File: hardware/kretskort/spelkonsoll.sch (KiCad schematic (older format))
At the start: 18 parts, among them SW1 SW_Push, SW2 SW_Push, SW3 SW_Push, SW4 SW_Push, SW5 SW_Push, SW6 SW_Push, SW7 SW_Push, SW8 SW_Push, U1 ESP32-DEVKITC-32D, U2 ILI9488

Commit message: update KiCad files
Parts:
- removed SW1, SW2, SW3, SW4, SW5, SW6, SW7, SW8: SW_Push, footprints:B3F1052, symbol spelkonsoll-rescue:SW_Push-Switch
- added SW1, SW2, SW3, SW4, SW5, SW6, SW7, SW8: B3F-1052, footprints:Button, symbol Button:B3F-1052
- added U3: 1043, footprints:18650holder, symbol 18650holder:1043
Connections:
- net +5V: now also SW1.3, SW2.3, SW3.3, SW4.3, SW5.3, SW6.3, SW7.3, SW8.3, U3.1
- net BTN_A: now also SW5.1
- net BTN_B: now also SW6.1
- net BTN_DP_DOWN: now also SW2.1
- net BTN_DP_LEFT: now also SW3.1
- net BTN_DP_RIGHT: now also SW4.1
- net BTN_DP_UP: now also SW1.1
- net BTN_X: now also SW7.1
- net BTN_Y: now also SW8.1
- net GND: now also U3.2
- no-connect marks 29 -> 45
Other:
- note added: "18650 BATTERY"
- note added: "BUTTONS"
- note removed: "BUTTONS ’N"
- moved on the sheet: R1, U1, U2

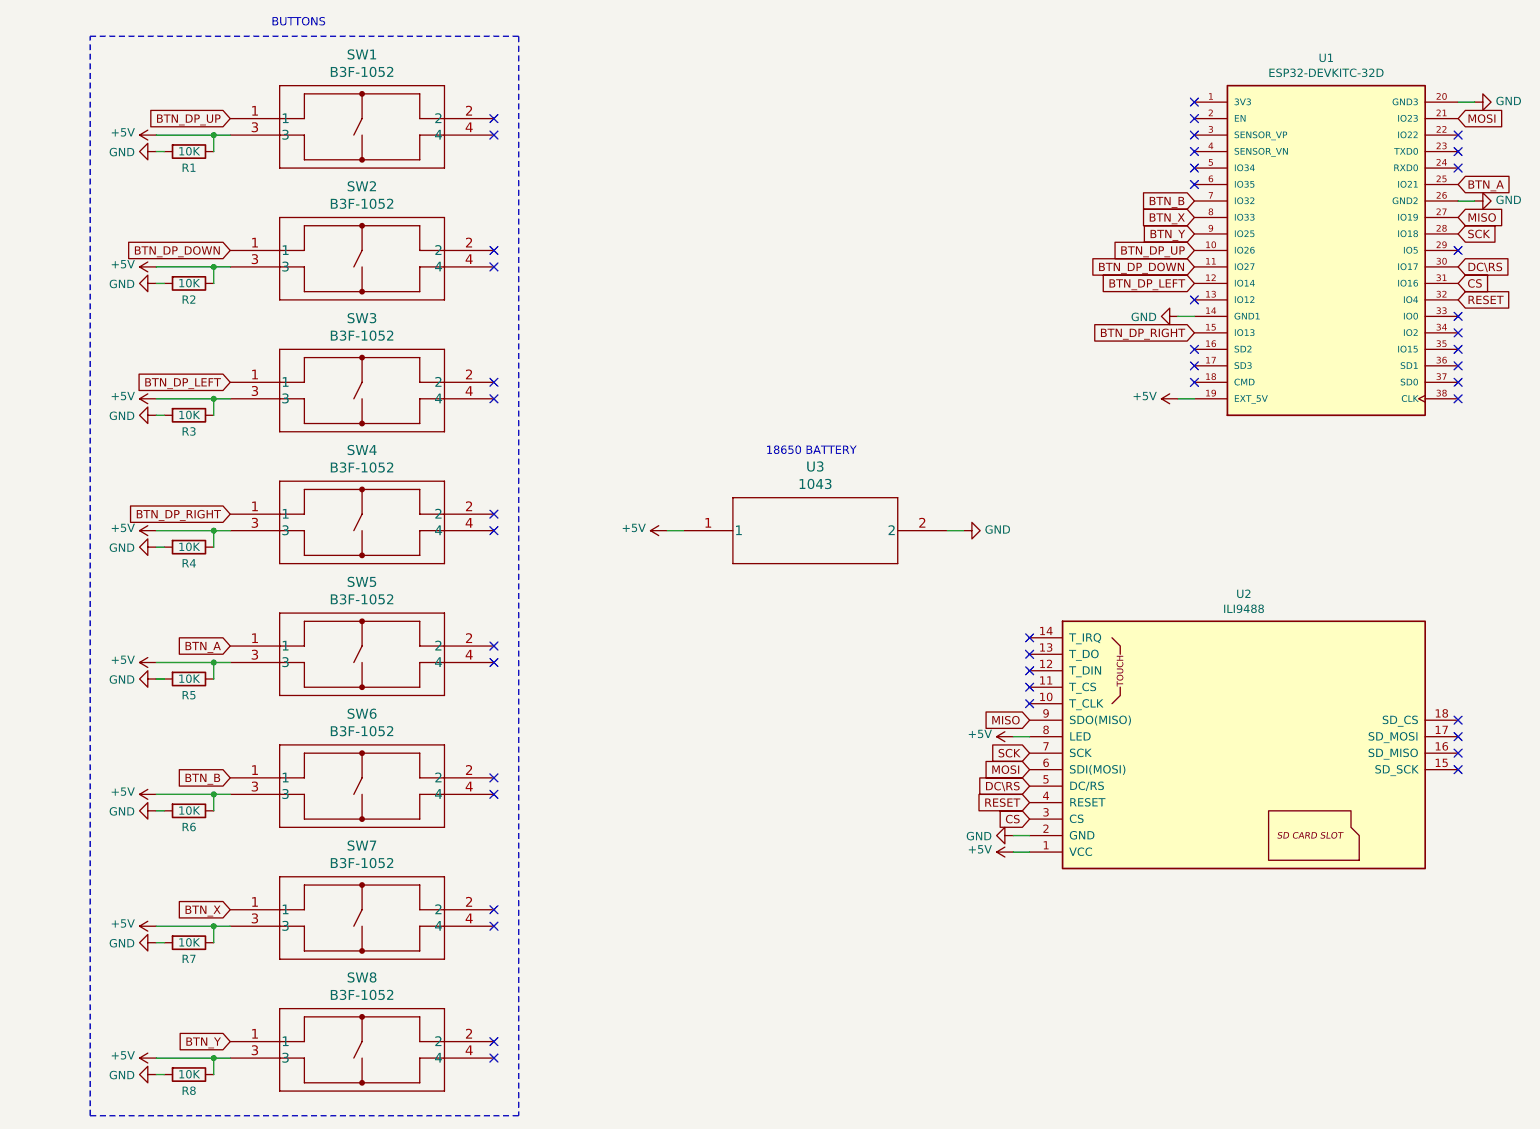
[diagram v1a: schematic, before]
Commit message: update schematic and footprints
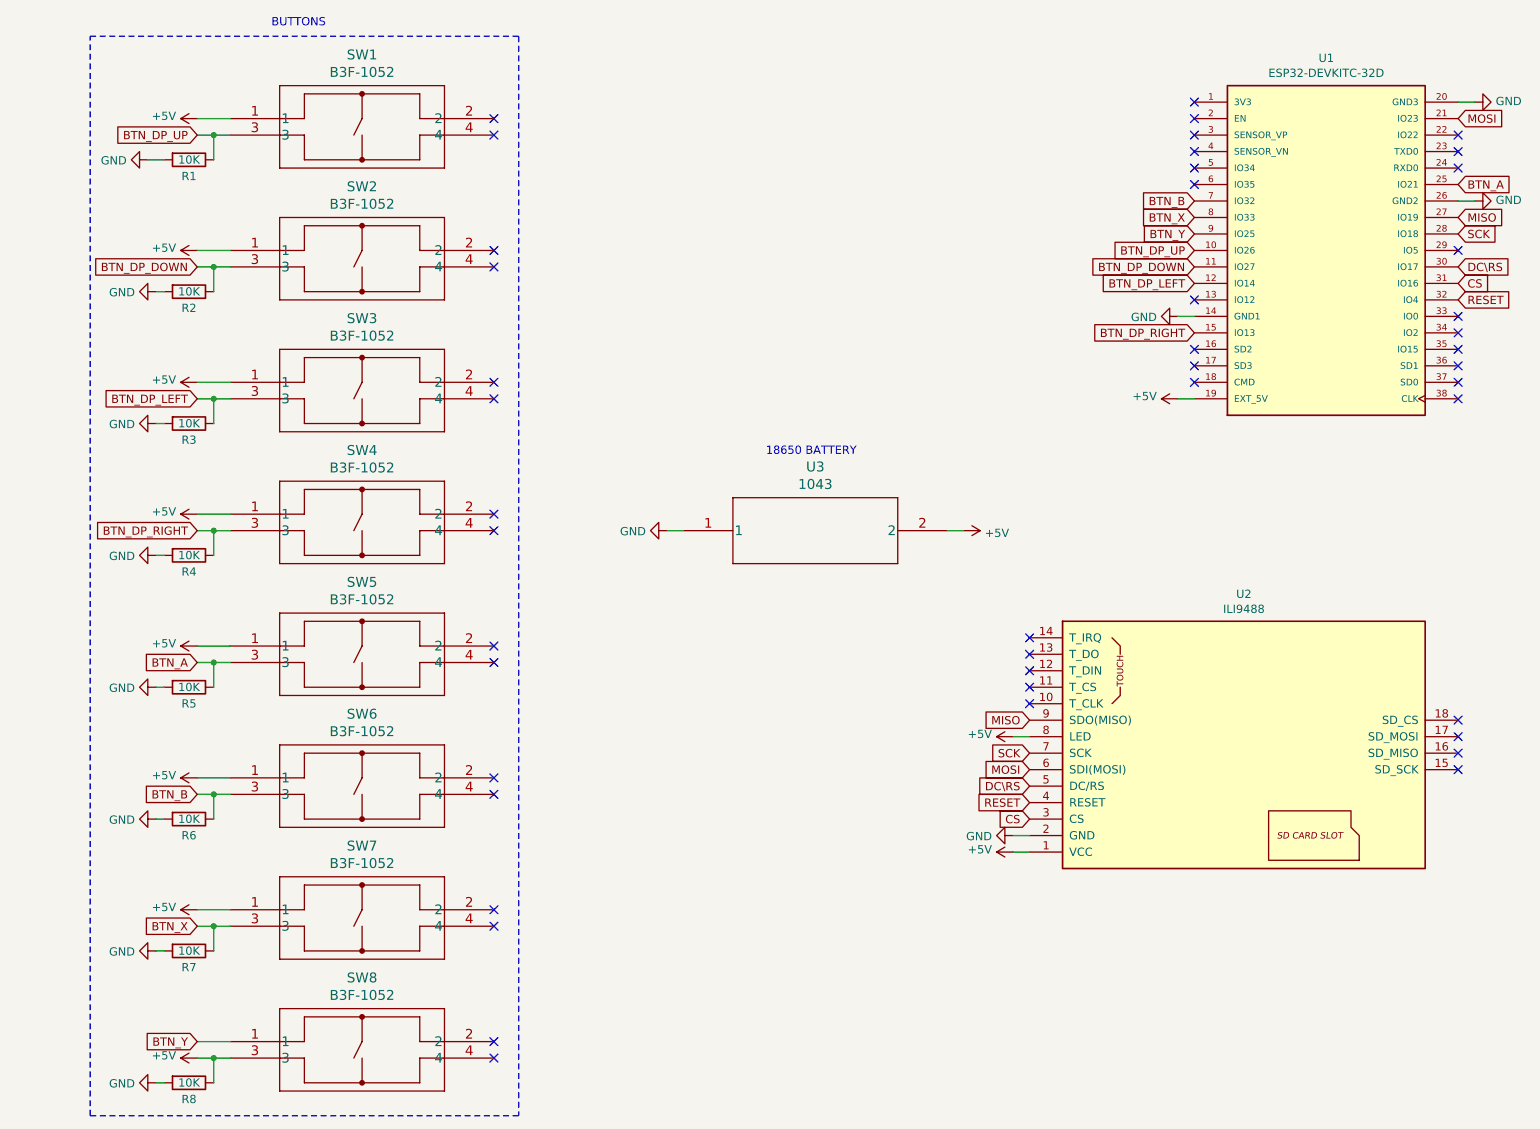
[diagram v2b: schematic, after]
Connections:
- net +5V: now also SW1.1, SW2.1, SW3.1, SW4.1, SW5.1, SW6.1, SW7.1, U3.2; no longer R1.1, R2.1, R3.1, R4.1, R5.1, R6.1, R7.1, SW1.3, SW2.3, SW3.3, SW4.3, SW5.3, SW6.3, SW7.3, U3.1
- net BTN_A: now also R5.1, SW5.3; no longer SW5.1
- net BTN_B: now also R6.1, SW6.3; no longer SW6.1
- net BTN_DP_DOWN: now also R2.1, SW2.3; no longer SW2.1
- net BTN_DP_LEFT: now also R3.1, SW3.3; no longer SW3.1
- net BTN_DP_RIGHT: now also R4.1, SW4.3; no longer SW4.1
- net BTN_DP_UP: now also R1.1, SW1.3; no longer SW1.1
- net BTN_X: now also R7.1, SW7.3; no longer SW7.1
- net GND: now also U3.1; no longer U3.2
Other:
- moved on the sheet: R1, R2, R3, R4, R5, R6, R7, R8

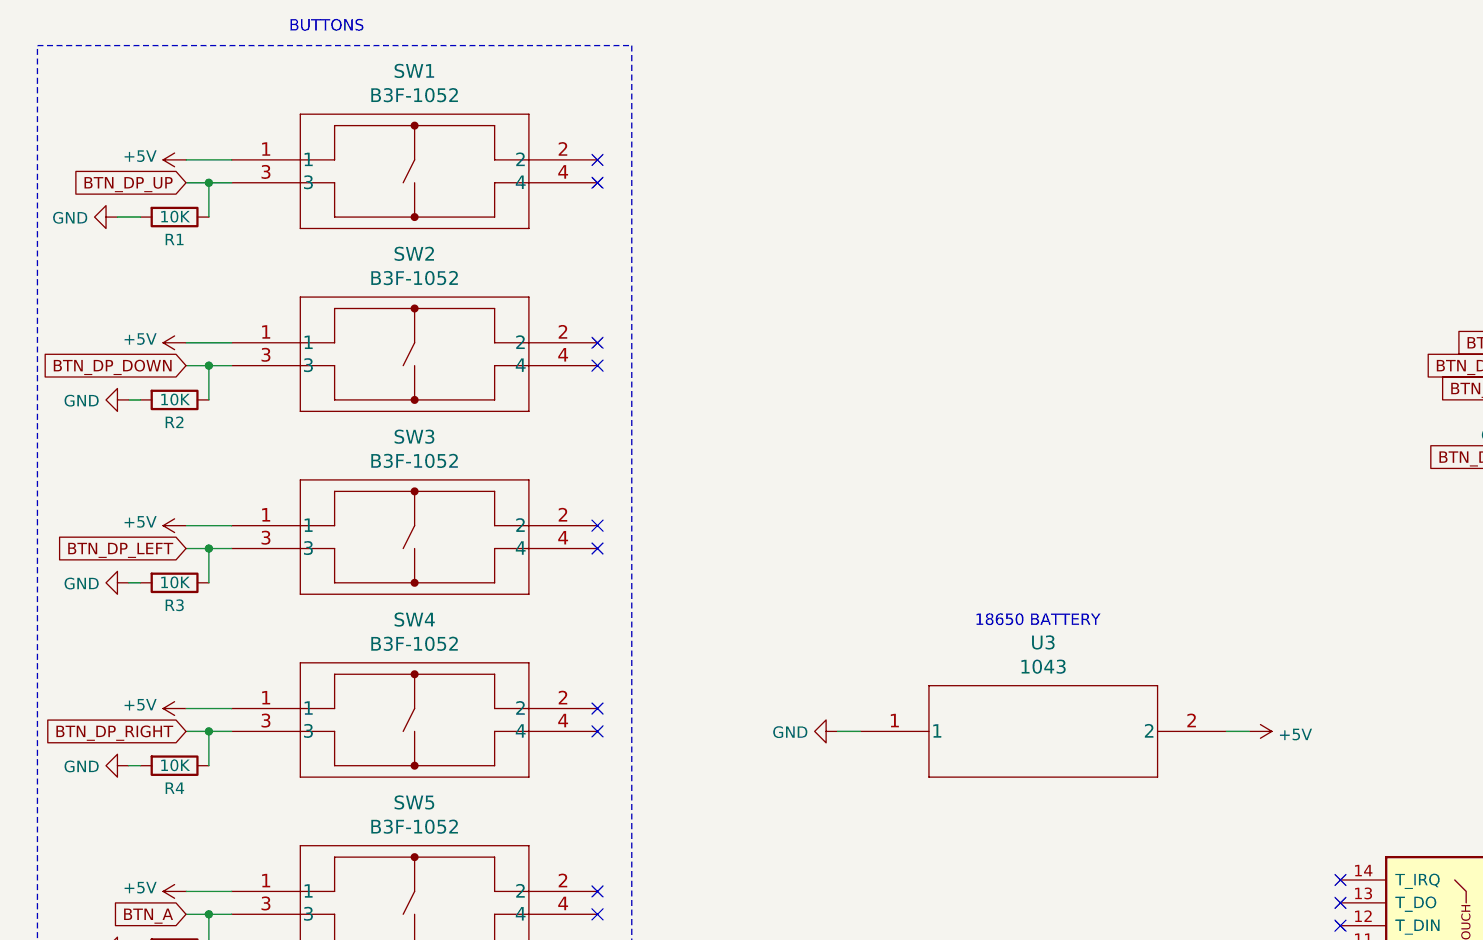
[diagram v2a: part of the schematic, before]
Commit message: added power switch
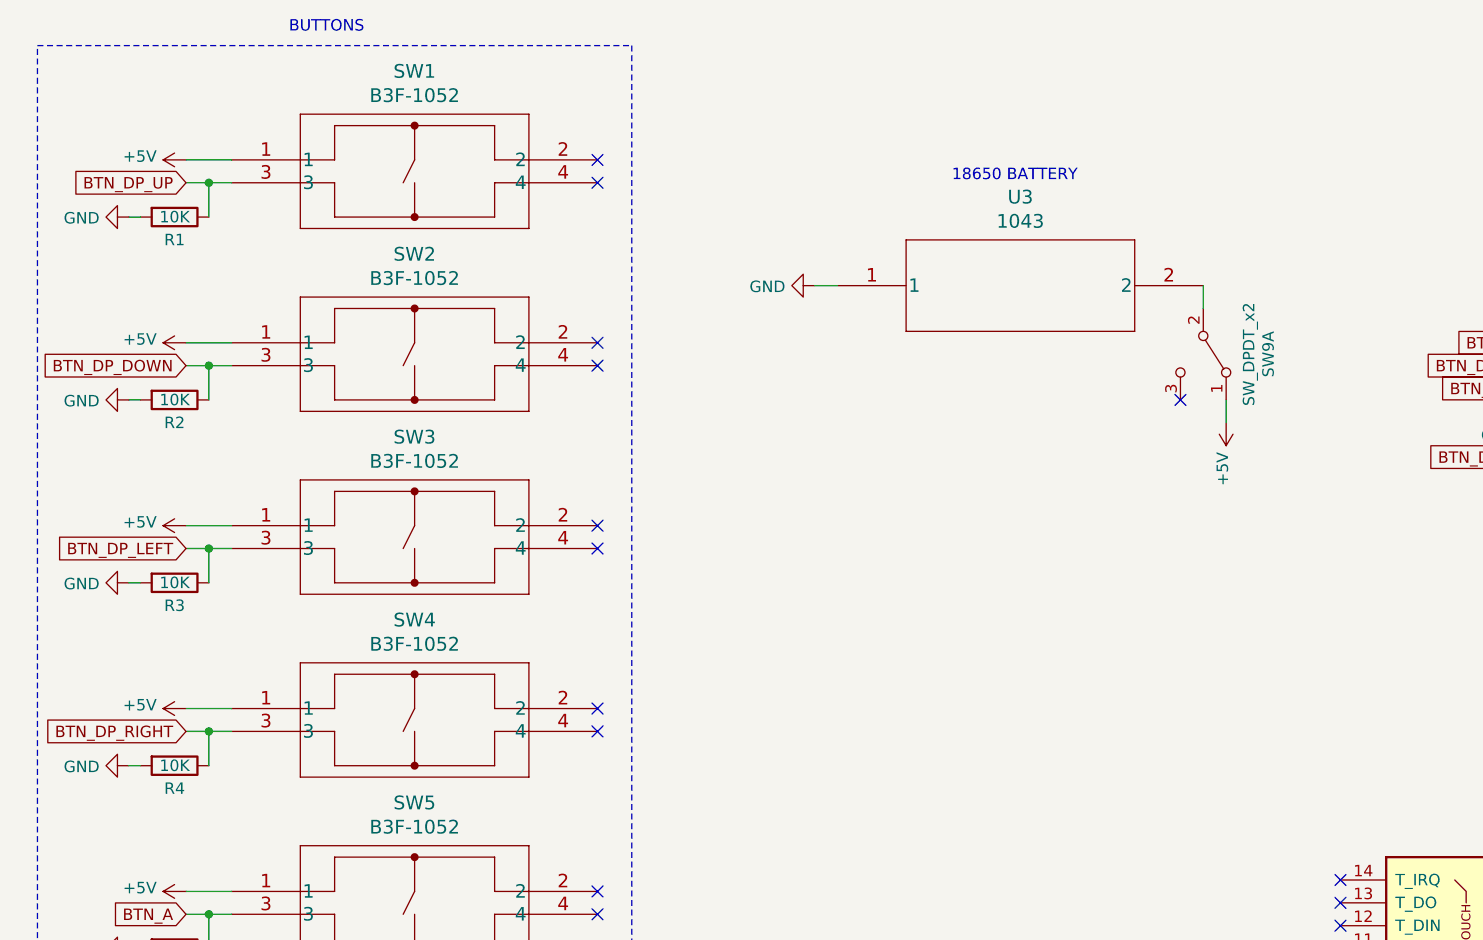
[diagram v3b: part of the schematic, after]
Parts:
- added SW9: SW_DPDT_x2, footprints:PowerButton, symbol Switch:SW_DPDT_x2
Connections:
- net +5V: now also SW9.1 (A); no longer U3.2
- new net: SW9.2 (B), U3.2
- no-connect marks 45 -> 46
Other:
- moved on the sheet: U3
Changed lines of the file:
@@
 L spelkonsoll-rescue:GND-power #PWR02
 U 1 1 624803D7
-P 2150 1600
-F 0 "#PWR02" H 2150 1350 50  0001 C CNN
-F 1 "GND" V 2155 1472 50  0000 R CNN
-F 2 "" H 2150 1600 50  0001 C CNN
-F 3 "" H 2150 1600 50  0001 C CNN
-	1    2150 1600
+P 2200 1600
+F 0 "#PWR02" H 2200 1350 50  0001 C CNN
+F 1 "GND" V 2205 1472 50  0000 R CNN
+F 2 "" H 2200 1600 50  0001 C CNN
+F 3 "" H 2200 1600 50  0001 C CNN
+	1    2200 1600
 	0    1    1    0
 $EndComp
@@
 NoConn ~ 4250 6950
 NoConn ~ 4250 7050
-Text Notes 5900 3400 0    50   ~ 0
+Text Notes 5800 1450 0    50   ~ 0
 18650 BATTERY
-$Comp
-L spelkonsoll-rescue:+5V-power #PWR0101
-U 1 1 63725E0B
-P 7100 3850
-F 0 "#PWR0101" H 7100 3700 50  0001 C CNN
-F 1 "+5V" V 7115 3978 50  0000 L CNN
-F 2 "" H 7100 3850 50  0001 C CNN
-F 3 "" H 7100 3850 50  0001 C CNN
-	1    7100 3850
-	0    1    1    0
-$EndComp
-$Comp
-L spelkonsoll-rescue:GND-power #PWR0102
-U 1 1 63726722
-P 5300 3850
-F 0 "#PWR0102" H 5300 3600 50  0001 C CNN
-F 1 "GND" V 5305 3722 50  0000 R CNN
-F 2 "" H 5300 3850 50  0001 C CNN
-F 3 "" H 5300 3850 50  0001 C CNN
-	1    5300 3850
-	0    1    1    0
-$EndComp
 $Comp
 L 18650holder:1043 U3
 U 1 1 6372E8C0
-P 5400 3850
-F 0 "U3" H 6200 4237 60  0000 C CNN
-F 1 "1043" H 6200 4131 60  0000 C CNN
-F 2 "footprints:18650holder" H 6200 4090 60  0001 C CNN
-F 3 "" H 5400 3850 60  0000 C CNN
-	1    5400 3850
+P 5300 1900
+F 0 "U3" H 6100 2287 60  0000 C CNN
+F 1 "1043" H 6100 2181 60  0000 C CNN
+F 2 "footprints:18650holder" H 6100 2140 60  0001 C CNN
+F 3 "" H 5300 1900 60  0000 C CNN
+	1    5300 1900
 	1    0    0    -1
 $EndComp
@@
 Wire Wire Line
 	2550 1450 2550 1600
-Wire Wire Line
-	2250 1600 2150 1600
 Wire Wire Line
 	2450 1450 2550 1450
@@
 Wire Wire Line
 	2250 4000 2200 4000
-Wire Wire Line
-	7000 3850 7100 3850
-Wire Wire Line
-	5400 3850 5300 3850
 $Comp
 L spelkonsoll-rescue:GND-power #PWR018
@@
 	0    -1   -1   0
 $EndComp
+Wire Wire Line
+	2200 1600 2250 1600
+Wire Wire Line
+	5300 1900 5200 1900
+$Comp
+L spelkonsoll-rescue:GND-power #PWR0102
+U 1 1 63726722
+P 5200 1900
+F 0 "#PWR0102" H 5200 1650 50  0001 C CNN
+F 1 "GND" V 5205 1772 50  0000 R CNN
+F 2 "" H 5200 1900 50  0001 C CNN
+F 3 "" H 5200 1900 50  0001 C CNN
+	1    5200 1900
+	0    1    1    0
+$EndComp
+Wire Wire Line
+	7000 2400 7000 2500
+$Comp
+L Switch:SW_DPDT_x2 SW9
+U 1 1 637FA6A8
+P 6900 2200
+F 0 "SW9" H 6900 2485 50  0000 C CNN
+F 1 "SW_DPDT_x2" H 6900 2400 50  0000 C CNN
+F 2 "footprints:PowerButton" H 6900 2200 50  0001 C CNN
+F 3 "" H 6900 2200 50  0001 C CNN
+	1    6900 2200
+	0    1    1    0
+$EndComp
+$Comp
+L spelkonsoll-rescue:+5V-power #PWR0101
+U 1 1 63725E0B
+P 7000 2500
+F 0 "#PWR0101" H 7000 2350 50  0001 C CNN
+F 1 "+5V" V 7015 2628 50  0000 L CNN
+F 2 "" H 7000 2500 50  0001 C CNN
+F 3 "" H 7000 2500 50  0001 C CNN
+	1    7000 2500
+	-1   0    0    1
+$EndComp
+Wire Wire Line
+	6900 1900 6900 2000
+NoConn ~ 6800 2400
 $EndSCHEMATC

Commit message: glemte å lagre :(
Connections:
- net +5V: now also SW9.3 (C); no longer SW9.1 (A)
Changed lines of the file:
@@
 $EndComp
 Wire Wire Line
-	7000 2400 7000 2500
+	6800 2400 6800 2500
 $Comp
 L Switch:SW_DPDT_x2 SW9
@@
 L spelkonsoll-rescue:+5V-power #PWR0101
 U 1 1 63725E0B
-P 7000 2500
-F 0 "#PWR0101" H 7000 2350 50  0001 C CNN
-F 1 "+5V" V 7015 2628 50  0000 L CNN
-F 2 "" H 7000 2500 50  0001 C CNN
-F 3 "" H 7000 2500 50  0001 C CNN
-	1    7000 2500
+P 6800 2500
+F 0 "#PWR0101" H 6800 2350 50  0001 C CNN
+F 1 "+5V" V 6815 2628 50  0000 L CNN
+F 2 "" H 6800 2500 50  0001 C CNN
+F 3 "" H 6800 2500 50  0001 C CNN
+	1    6800 2500
 	-1   0    0    1
 $EndComp
 Wire Wire Line
 	6900 1900 6900 2000
-NoConn ~ 6800 2400
+NoConn ~ 7000 2400
 $EndSCHEMATC

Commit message: må slutte å glemme å lagre :(
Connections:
- net +5V: now also U1.1 (3V3); no longer U1.19 (EXT_5V)
- no-connect marks 46 -> 45
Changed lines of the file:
@@
 	1    0    0    -1
 $EndComp
-$Comp
-L spelkonsoll-rescue:+5V-power #PWR021
-U 1 1 61F50C10
-P 8400 3050
-F 0 "#PWR021" H 8400 2900 50  0001 C CNN
-F 1 "+5V" V 8415 3178 50  0000 L CNN
-F 2 "" H 8400 3050 50  0001 C CNN
-F 3 "" H 8400 3050 50  0001 C CNN
-	1    8400 3050
-	0    -1   -1   0
-$EndComp
-Wire Wire Line
-	8500 3050 8400 3050
+Wire Wire Line
+	8500 1250 8400 1250
 $Comp
 L spelkonsoll-rescue:GND-power #PWR022
@@
 Text GLabel 8500 2650 0    50   Input ~ 0
 BTN_DP_RIGHT
-NoConn ~ 8500 1250
 NoConn ~ 8500 1350
 NoConn ~ 8500 1450
@@
 	6900 1900 6900 2000
 NoConn ~ 7000 2400
+$Comp
+L spelkonsoll-rescue:+5V-power #PWR021
+U 1 1 61F50C10
+P 8400 1250
+F 0 "#PWR021" H 8400 1100 50  0001 C CNN
+F 1 "+5V" V 8415 1378 50  0000 L CNN
+F 2 "" H 8400 1250 50  0001 C CNN
+F 3 "" H 8400 1250 50  0001 C CNN
+	1    8400 1250
+	0    -1   -1   0
+$EndComp
 $EndSCHEMATC
